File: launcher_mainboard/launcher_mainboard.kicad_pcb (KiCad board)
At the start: 4 copper layers, 87.5 x 89 mm, 80 parts, among them J10 header, J11 header, J12 USB_C_Receptacle_USB2.0_16P, J2 Conn_01x06, J3 Conn_01x06, J4 Conn_01x06, J5 Conn_01x06, J6 bat_con, J7 fan_con, J8 ESC_1, J9 ESC_2, Q1 2N7002H, Q2 MMBT3904, Q3 MMBT3904, Q4 BSS138, Q5 BSS138, Q6 BSS138, Q7 BSS138, SW1 POWER_SWITCH, U10 TLV75533PDBV, U12 LM66200DRLR, U2 TMC2209-LA-T, U3 TMC2209-LA-T, U4 TMC2209-LA-T, U5 TMC2209-LA-T, U6 ESP32-S3-WROOM-1, U7 R-78E3.3-0.5, U8 D3V3XA4B10LP, U9 R-78E5.0-0.5

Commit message: more layout
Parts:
- C10, C11, C12, C9: footprint Capacitor_SMD:CP_Elec_3x5.3 -> Capacitor_SMD:CP_Elec_8x10.5
- moved C7 20.0 mm to (99.0, 82.5)
- moved C8 20.0 mm to (99.0, 86.5)
- moved J2 13.2 mm to (156.0, 68.0), turned to 180 degrees
- moved J4 12.9 mm to (156.0, 114.0), turned to 180 degrees
- moved J5 12.9 mm to (156.0, 136.5), turned to 180 degrees
- moved J3 12.5 mm to (156.0, 90.5), turned to 180 degrees
- moved D5 9.47 mm to (114.4, 83.5)
- moved C12 6.19 mm to (150.5, 125.0), turned to 0 degrees
- moved U6 6.02 mm to (111.8, 62.7)
- moved R5 6.00 mm to (124.5, 59.6)
- moved C11 5.48 mm to (150.5, 56.5), turned to 0 degrees
- moved C9 5.18 mm to (150.3, 102.0), turned to 0 degrees
- moved C10 4.36 mm to (150.5, 78.0), turned to 0 degrees
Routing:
- net /PDN_UART: track 123.9 -> 11.0 mm
- net +BATT: track 0.00 -> 28.9 mm
- net /M3_A2: track 7.83 -> 22.0 mm
- net /M4_A2: track 7.78 -> 21.3 mm
- net /M2_A2: track 7.77 -> 20.9 mm
- net /M1_A2: track 7.74 -> 20.4 mm
- net /M1_A1: track 8.32 -> 16.3 mm
- net /M2_A1: track 8.38 -> 15.8 mm
- net /M3_A1: track 8.44 -> 15.8 mm
- net /M4_A1: track 8.29 -> 15.4 mm
- net /M4_DIR: track 76.2 -> 69.5 mm
- net /M4_STEP: track 75.0 -> 68.4 mm
- net /M3_DIR: track 56.0 -> 49.5 mm
- net /M3_STEP: track 54.6 -> 48.3 mm
- net /M2_DIR: track 35.6 -> 29.4 mm
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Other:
- board size 87.5 x 89 mm -> 93.1 x 91.5 mm

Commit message: more layout
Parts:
- removed Q2, Q3: MMBT3904, Package_TO_SOT_SMD:SOT-23
- removed R11, R13: 10k, Resistor_SMD:R_0805_2012Metric
- removed U7: R-78E3.3-0.5, Converter_DCDC:Converter_DCDC_RECOM_R-78E-0.5_THT
- added .: LOGO, CustomFootprints:birdie_img, F.Cu at (101.0, 89.5)
- added U1: R-78E3.3-1.0, Converter_DCDC:Converter_DCDC_RECOM_R-78E-0.5_THT, F.Cu at (99.6, 117.7)
- D1, D4, D5: footprint LED_SMD:LED_PLCC-2_3x2mm_AK -> LED_SMD:LED_0805_2012Metric
- D2: footprint Diode_SMD:D_0201_0603Metric -> Diode_SMD:D_0805_2012Metric
- D6: footprint Diode_THT:D_DO-35_SOD27_P5.08mm_Vertical_KathodeUp -> Diode_SMD:D_0805_2012Metric
- J7: footprint Connector_Molex:Molex_PicoBlade_53047-0210_1x02_P1.25mm_Vertical -> Connector_JST:JST_XH_B2B-XH-A_1x02_P2.50mm_Vertical
- Q1: value 2N7002H -> PJC7400; footprint Package_TO_SOT_SMD:SOT-23 -> Package_TO_SOT_SMD:SOT-323_SC-70
- R9: value 1.5k -> 680
- moved R8 56.8 mm to (113.5, 88.0), turned to 0 degrees
- moved R9 55.6 mm to (113.5, 85.0), turned to 180 degrees
- moved Q1 41.8 mm to (113.3, 92.5), turned to -90 degrees
- moved J7 40.7 mm to (120.5, 99.5), turned to 180 degrees
- moved R3 29.7 mm to (119.5, 94.0), turned to 180 degrees
- moved R12 28.0 mm to (119.5, 79.0)
- moved C15 27.8 mm to (115.5, 121.5)
- moved J8 26.6 mm to (118.0, 135.1)
- moved J6 25.9 mm to (92.0, 135.1)
- moved C16 25.7 mm to (120.5, 109.0)
- moved C7 24.5 mm to (100.0, 58.0), turned to -90 degrees
- moved C8 24.5 mm to (100.0, 62.0), turned to 90 degrees
- moved U9 23.7 mm to (114.1, 117.7)
- moved D1 22.9 mm to (119.5, 91.0)
- moved R6 22.6 mm to (116.5, 106.4), turned to -90 degrees
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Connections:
- D4 pad 1: Net-(D4-K) -> -BATT
- D5 pad 1: Net-(D5-K) -> -BATT
- R10 pad 1: +3.3V -> /ind_LED_1
- R12 pad 1: +3.3V -> /ind_LED_2
- R3 pad 2: /3.3VUSB -> +3.3V
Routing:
- net /PDN_UART: track 11.0 -> 98.6 mm
- net /motor_en: track 0.00 -> 83.6 mm, vias 0 -> 1
- net -BATT: track 0.00 -> 60.5 mm, vias 0 -> 17
- net +3.3V: track 0.00 -> 39.2 mm, vias 0 -> 6
- net /bat_volt_adc: track 0.00 -> 38.8 mm, vias 0 -> 2
- net +BATT: track 28.9 -> 66.1 mm
- net /+5VUSB: track 0.00 -> 27.6 mm, vias 0 -> 3
- net /+3.3VBatt: track 0.00 -> 14.6 mm
- net /ind_LED_1: track 0.00 -> 14.3 mm
- net Net-(D6-A): track 0.00 -> 10.7 mm
- net /fan_ctrl: track 0.00 -> 10.3 mm
- net +5V: track 0.00 -> 8.36 mm
- net /3.3VUSB: track 0.00 -> 7.47 mm
- net /USB_D-: track 0.00 -> 7.01 mm
- net Net-(Q1-G): track 0.00 -> 6.67 mm
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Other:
- board size 93.1 x 91.5 mm -> 88 x 91 mm

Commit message: more layout
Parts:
- moved R4 40.3 mm to (98.5, 94.0)
- moved BOOT1 33.8 mm to (102.0, 92.2)
- moved C5 24.8 mm to (98.8, 82.8)
- moved RESET1 19.6 mm to (98.5, 88.2)
- moved C8 4.72 mm to (97.5, 58.0), turned to -90 degrees
- moved R29 1.42 mm to (89.8, 63.8), turned to -90 degrees
- moved R28 1.17 mm to (89.8, 67.5), turned to -90 degrees
- moved R27 0.92 mm to (89.8, 71.2), turned to -90 degrees
- moved R26 0.68 mm to (89.8, 75.0), turned to -90 degrees
- moved R22 0.47 mm to (89.8, 90.0), turned to -90 degrees
- moved R25 0.44 mm to (89.8, 78.8), turned to -90 degrees
- moved R23 0.26 mm to (89.8, 86.2), turned to -90 degrees
- moved R24 0.24 mm to (89.8, 82.5), turned to -90 degrees
- turned R15 to 180 degrees
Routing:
- net +5V: track 8.36 -> 110.1 mm, vias 0 -> 2
- net /TXD0: track 0.00 -> 50.5 mm, vias 0 -> 1
- net /RXD0: track 0.00 -> 46.4 mm, vias 0 -> 1
- net /USB_D-: track 7.01 -> 51.0 mm
- net /USB_D+: track 4.86 -> 48.9 mm
- net /LV1: track 0.00 -> 39.3 mm, vias 0 -> 2
- net /LV4: track 0.00 -> 38.2 mm, vias 0 -> 2
- net /LV3: track 0.00 -> 34.3 mm, vias 0 -> 2
- net /LV2: track 0.00 -> 33.9 mm, vias 0 -> 2
- net /HV_SIGNAL_1: track 0.00 -> 32.3 mm, vias 0 -> 1
- net /IO_EXTRA_3: track 0.00 -> 31.4 mm, vias 0 -> 1
- net /IO_EXTRA_1: track 0.00 -> 31.4 mm, vias 0 -> 1
- net /IO_EXTRA_5: track 0.00 -> 31.4 mm, vias 0 -> 1
- net /HV4: track 0.00 -> 28.1 mm
- net /IO_EXTRA_6: track 0.00 -> 27.5 mm, vias 0 -> 1
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
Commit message: project restructure, switched out EDC IC, more layout
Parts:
- removed U8: D3V3XA4B10LP, Package_DFN_QFN:Diodes_UDFN-10_1.0x2.5mm_P0.5mm
- added D3: DT1042-04SO-7, DT1042:SOT95P285X140-6N, F.Cu at (84.5, 104.5)
- moved . 51.9 mm to (49.2, 92.4)
- moved BOOT1 10.8 mm to (109.0, 84.0)
- moved C5 8.53 mm to (103.2, 90.0)
- moved RESET1 6.56 mm to (103.5, 84.0)
- moved R4 4.85 mm to (103.2, 93.0)
- moved U10 0.50 mm to (93.5, 104.0)
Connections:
- J12 pad S1: -BATT -> unconnected-(J12-SHIELD-PadS1)_2
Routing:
- net Net-(U6-EN): track 0.00 -> 36.0 mm, vias 0 -> 2
- net /PDN_UART: track 98.6 -> 82.7 mm
- net Net-(U6-IO0): track 0.00 -> 14.3 mm, vias 0 -> 2
- net -BATT: track 82.0 -> 89.1 mm, vias 25 -> 28
- net /+5VUSB: track 27.6 -> 29.8 mm, vias 3 -> 2
- net /LV2: track 33.9 -> 35.9 mm
- net /USB_D-: track 51.0 -> 52.6 mm
- net +3.3V: track 58.6 -> 59.6 mm, vias 12 -> 13

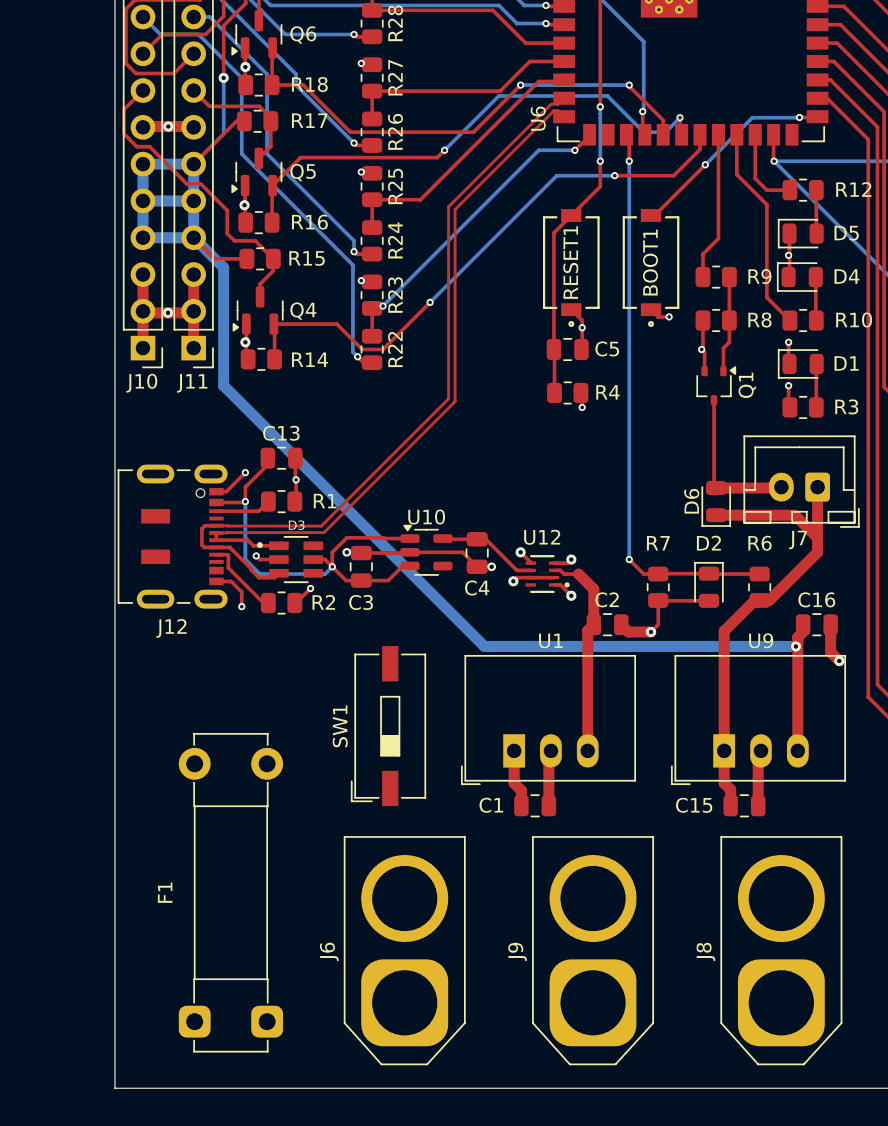
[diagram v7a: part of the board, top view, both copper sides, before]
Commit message: renamed folder. How do differential pairs work?
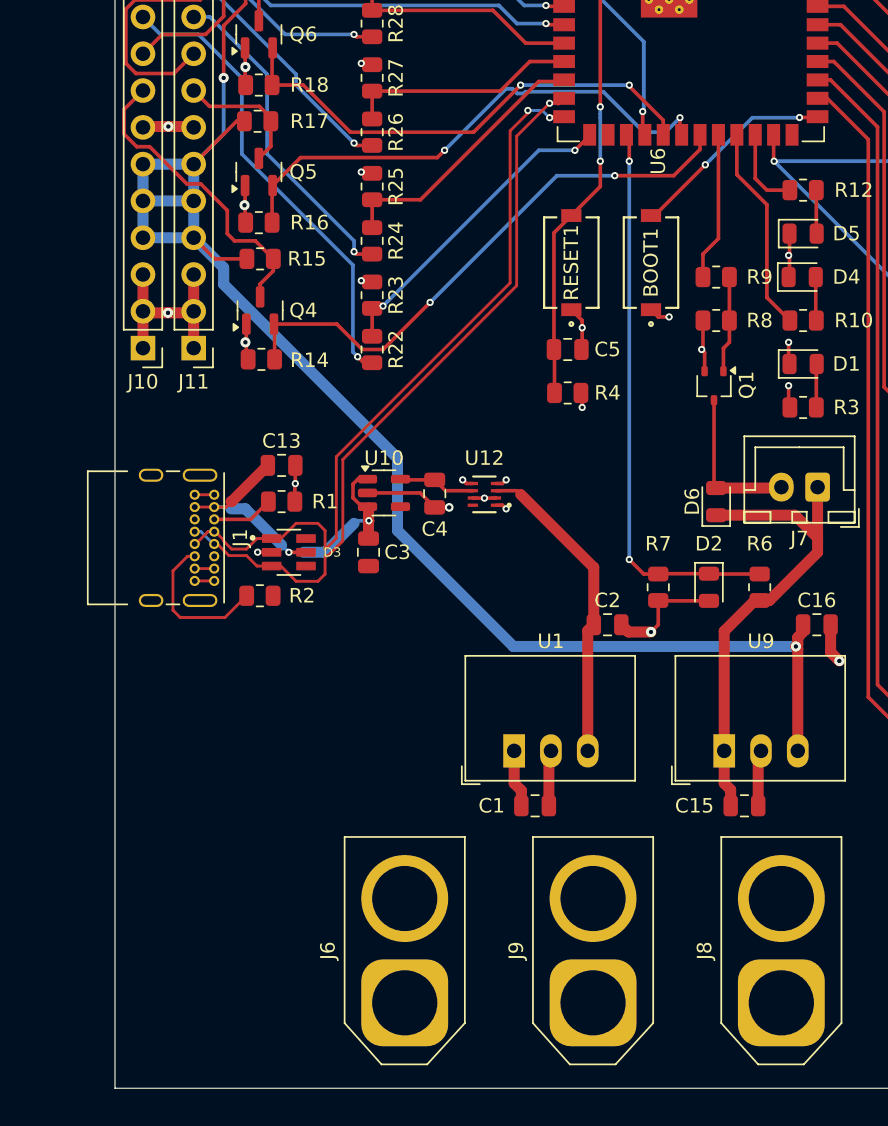
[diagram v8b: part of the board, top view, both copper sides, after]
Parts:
- removed F1: Fuse, Fuse:Fuseholder_Clip-5x20mm_Bel_FC-203-22_Lateral_P17.80x5.00mm_D1.17mm_Horizontal
- removed J12: USB_C_Receptacle_USB2.0_16P, Connector_USB:USB_C_Receptacle_JAE_DX07S016JA1R1500
- removed SW1: POWER_SWITCH, Button_Switch_SMD:SW_DIP_SPSTx01_Slide_9.78x4.72mm_W8.61mm_P2.54mm
- added J1: USB_C_Receptacle_USB2.0_16P, Connector_USB:USB_C_Receptacle_GCT_USB4085, F.Cu at (78.8, 100.0)
- moved U12 6.80 mm to (97.5, 100.0)
- moved C4 5.04 mm to (94.1, 100.0)
- moved U10 5.04 mm to (90.6, 99.9)
- moved R2 1.58 mm to (82.0, 107.0)
- moved C3 1.12 mm to (89.5, 104.0), turned to -90 degrees
- moved D3 0.71 mm to (84.0, 104.0)
- moved C13 0.50 mm to (83.5, 98.0)
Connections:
- J6 pad 2: Net-(J6-Pin_2) -> +BATT
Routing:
- net -BATT: track 89.1 -> 78.7 mm, vias 28 -> 24
- net /+3.3VBatt: track 14.6 -> 21.8 mm
- net Net-(J1-CC2): track 5.48 -> 10.6 mm
- net /+5VUSB: track 29.8 -> 27.2 mm
- net /USB_D+: track 49.0 -> 51.1 mm, vias 0 -> 2
- net /USB_D-: track 52.6 -> 50.9 mm, vias 0 -> 1
- net +3.3V: track 59.6 -> 58.3 mm
- net +5V: track 110.1 -> 108.9 mm
- net /3.3VUSB: track 7.47 -> 6.42 mm
- net /LV2: track 35.9 -> 36.5 mm
